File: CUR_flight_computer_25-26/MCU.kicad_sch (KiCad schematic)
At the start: 27 parts, among them SW1 GSPTS0018, SW2 SW_SPDT, Y1 ECS-250-18-36B2-CTY

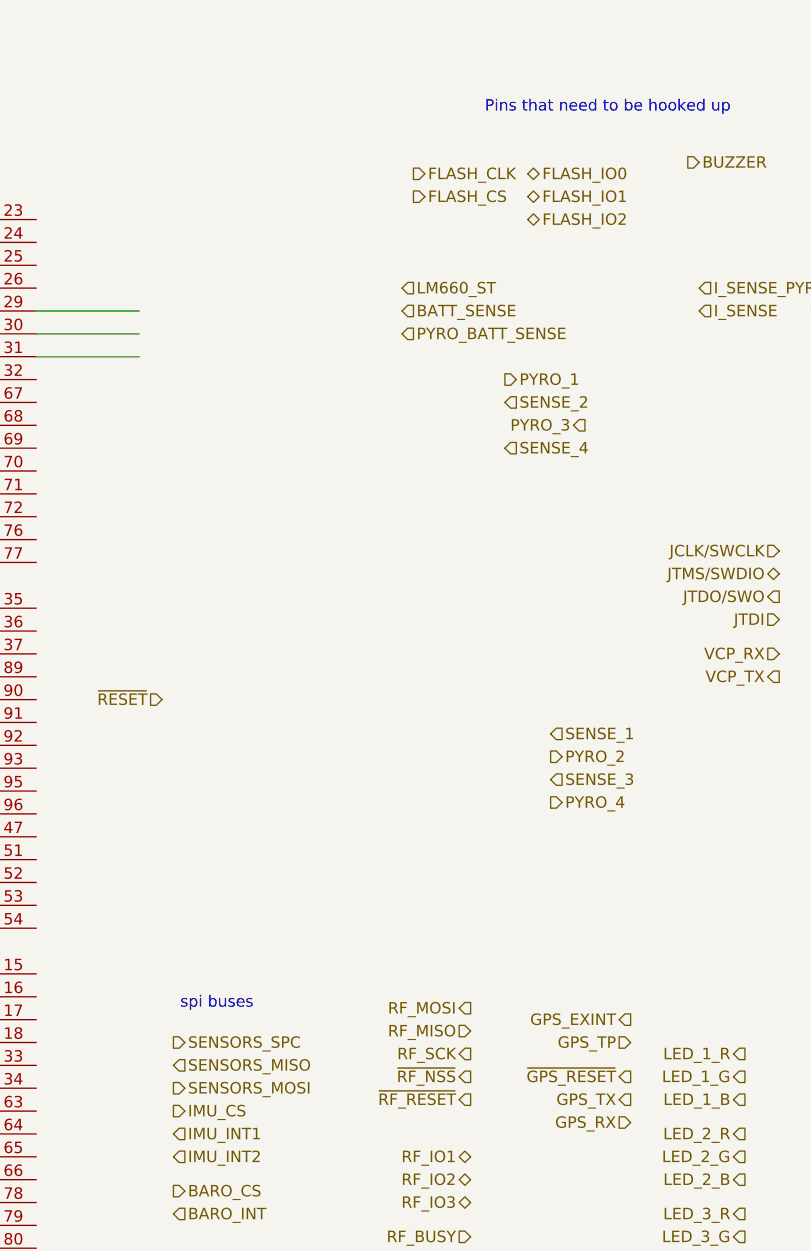
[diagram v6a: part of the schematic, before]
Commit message: slight pin name changes
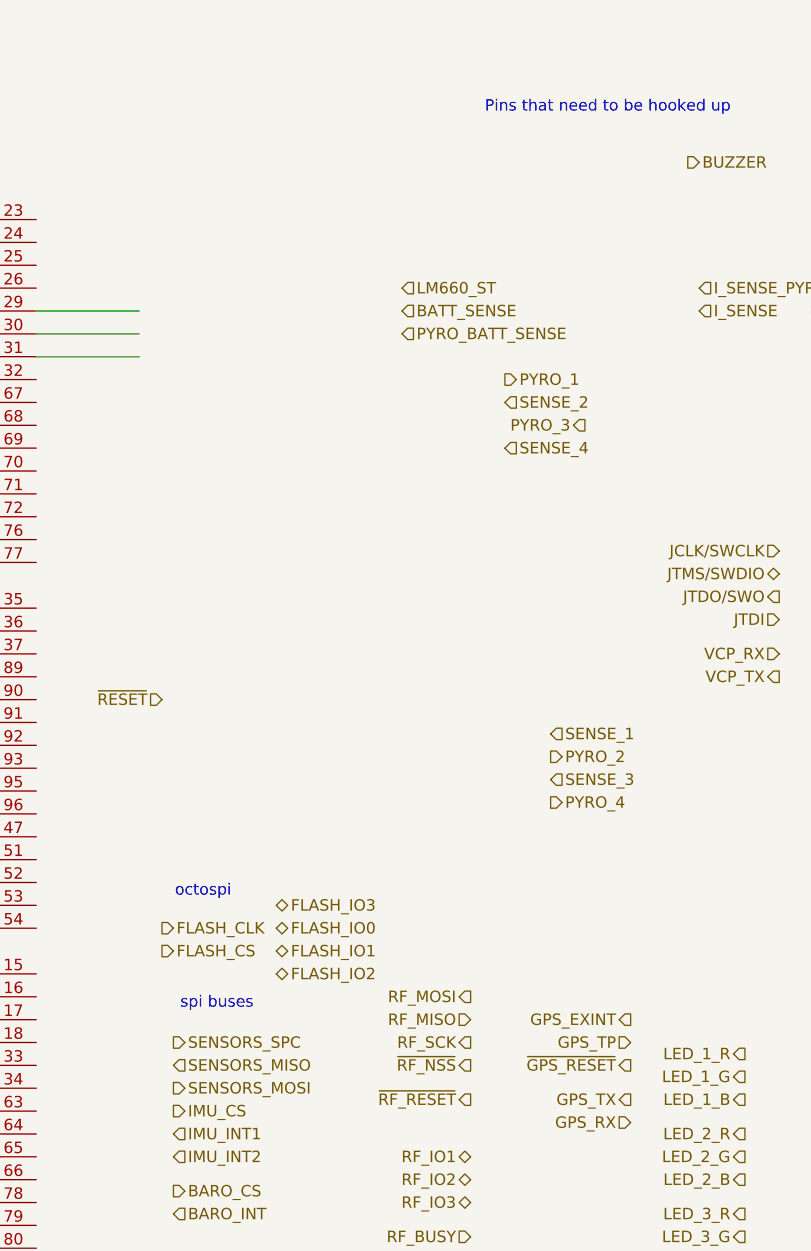
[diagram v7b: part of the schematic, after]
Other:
- note added: "octospi"

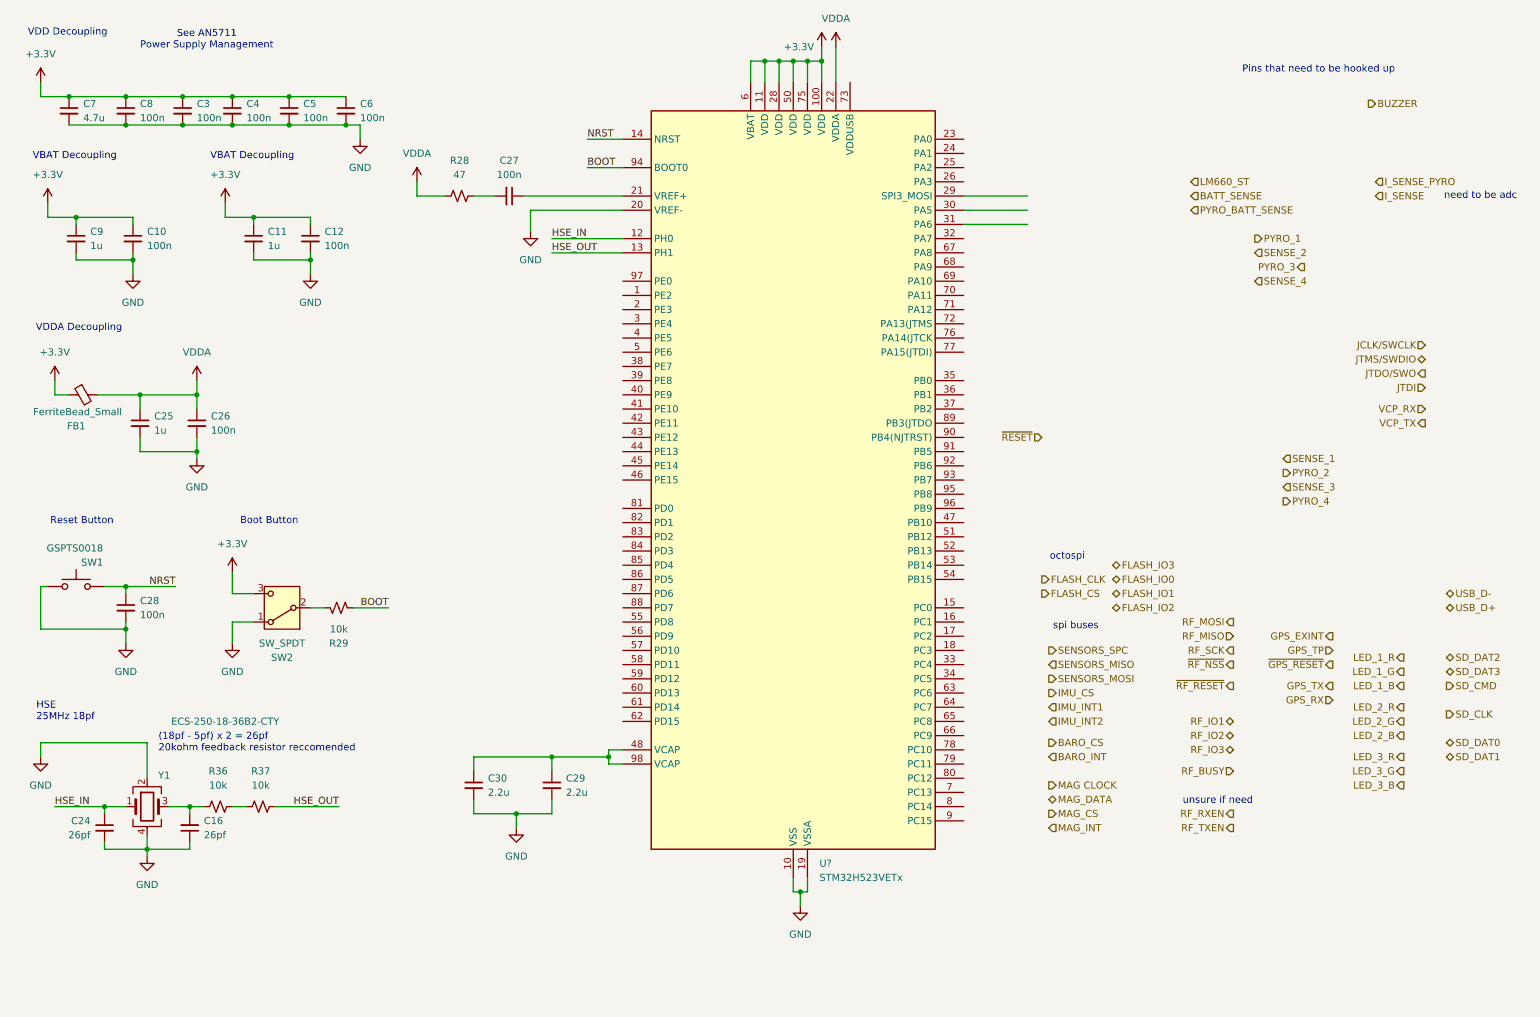
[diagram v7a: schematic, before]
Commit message: more pin hooking up work
spi
2- sensors
3- mag
4- rf

uart5- debug
uart4- gps

hooked up sd card using sdmmc
hooked up debug

to do:
- pyro activation/sense lines
- battery sensing
- rf io pins
- interrupt
- baro/imu cs pins
- leds
-buttons
- buzzer
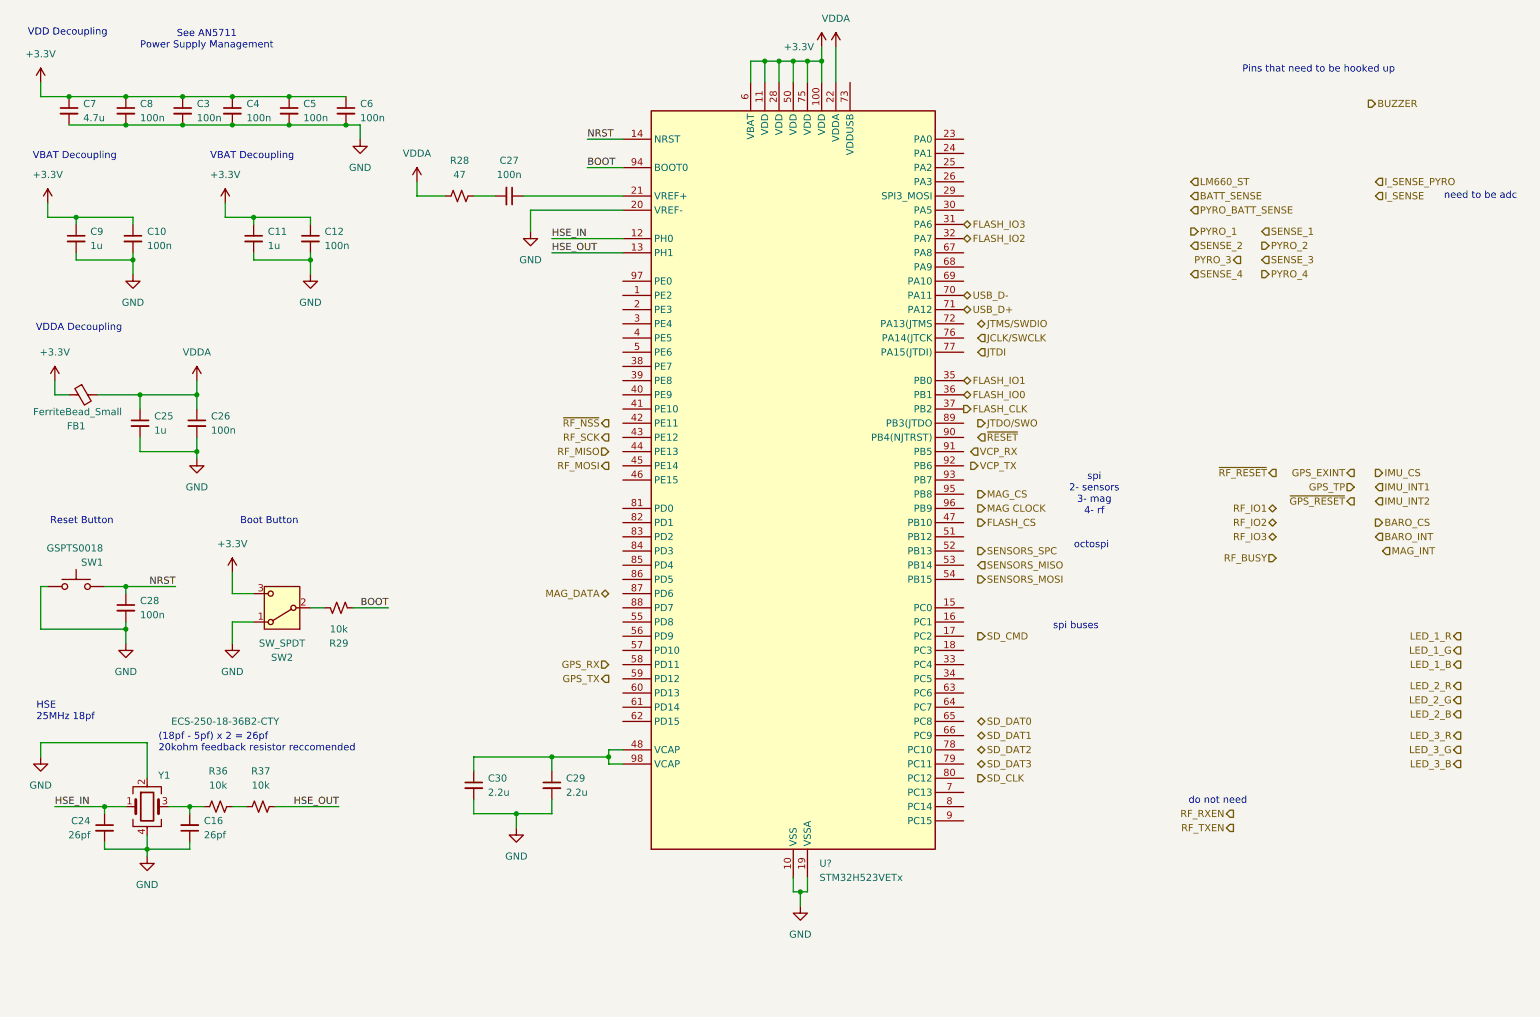
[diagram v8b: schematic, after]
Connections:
- net FLASH_CLK: now also U?.37 (PB2)
- net FLASH_IO0: now also U?.36 (PB1)
- net FLASH_IO1: now also U?.35 (PB0)
- net FLASH_IO2: now also U?.32 (PA7)
- net FLASH_IO3: now also U?.31 (PA6)
- net USB_D+: now also U?.71 (PA12)
- net USB_D-: now also U?.70 (PA11)
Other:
- note added: "do not need"
- note added: "spi 2- sensors 3- mag 4- rf"
- note removed: "unsure if need"
